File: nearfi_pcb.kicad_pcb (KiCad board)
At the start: 4 copper layers, 45.6 x 45.6 mm, 50 parts, among them J1 PWR_CNN, J2 PROG_CNN, Q1 MMBT3904, SW1 SRST_BTN, U2 TLV1117-33, U3 AT24CS02-STUM, U4 TPL5010, U5 ESP32-S3-MINI-1

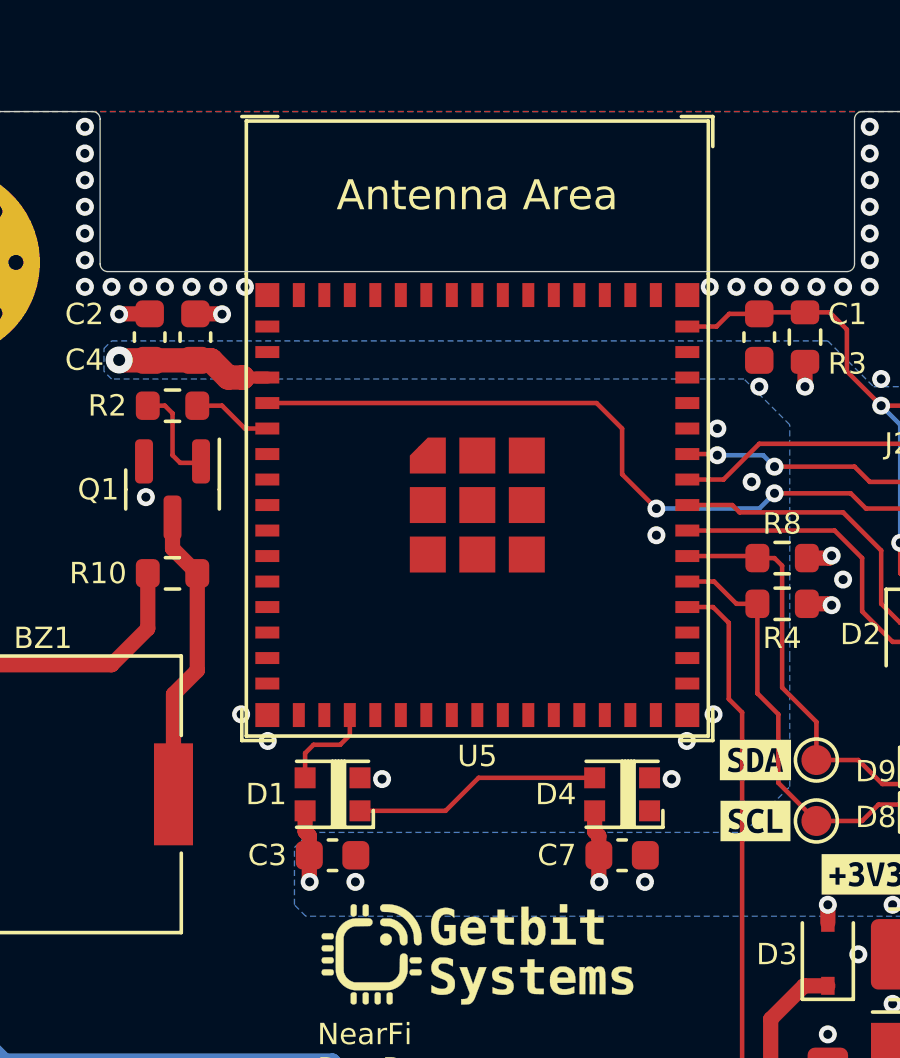
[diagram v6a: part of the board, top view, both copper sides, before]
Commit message: updated to work with kicad v8
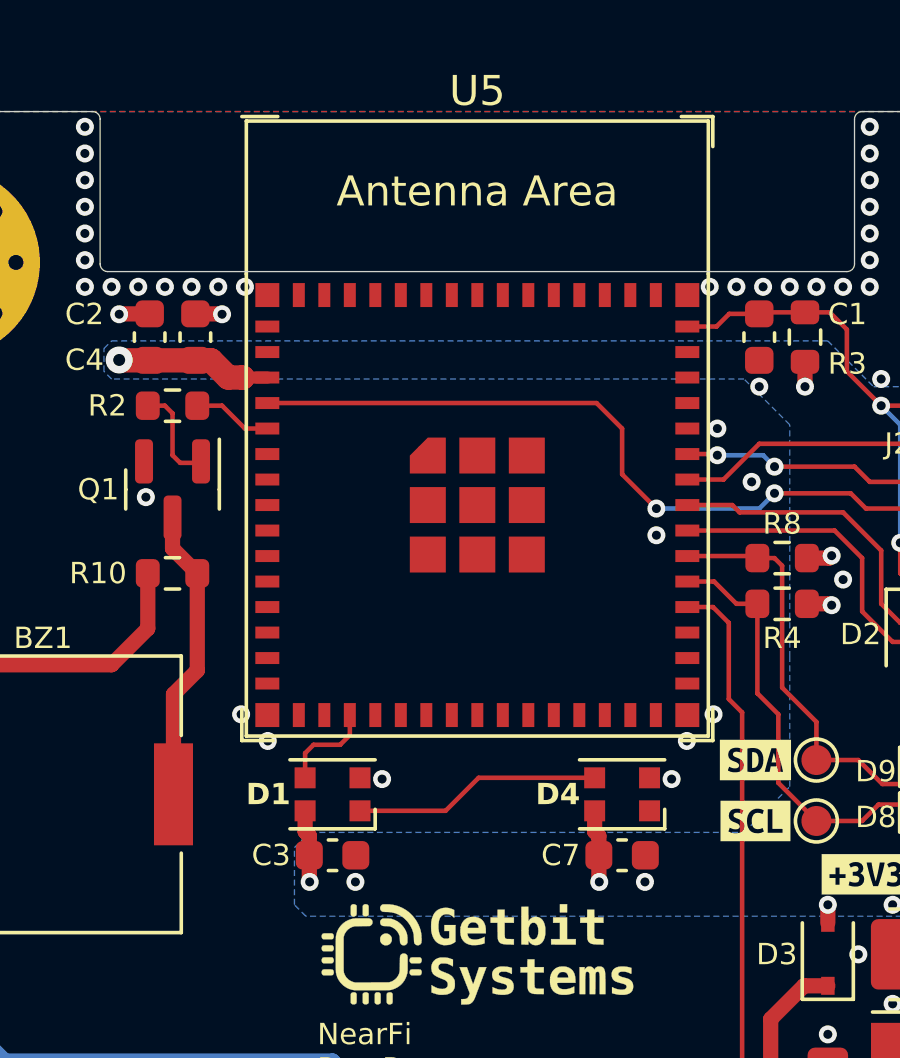
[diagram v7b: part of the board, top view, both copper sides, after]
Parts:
- D1, D4: footprint Misc:WS2812B-2020 -> LED_SMD:LED_WS2812B-2020_PLCC4_2.0x2.0mm
- U5: footprint Espressif:ESP32-S3-MINI-1 -> PCM_Espressif:ESP32-S3-MINI-1
- turned D1 to 180 degrees
- turned D4 to 180 degrees

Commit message: updated schematic and layout
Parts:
- moved C6 35.7 mm to (161.8, 103.9)
- moved D3 35.7 mm to (158.0, 103.9)
- moved D6 35.7 mm to (166.4, 104.6)
- moved G*** 35.7 mm to (146.3, 103.9)
- moved R6 35.7 mm to (156.0, 113.5)
- moved R7 35.7 mm to (166.4, 103.1)
- moved BZ1 35.7 mm to (131.8, 98.5)
- moved C1 35.7 mm to (155.7, 83.3)
- moved C10 35.7 mm to (167.1, 98.5)
- moved C2 35.7 mm to (135.4, 83.3)
- moved C4 35.7 mm to (136.9, 83.3)
- moved D1 35.7 mm to (141.5, 98.5)
- moved D4 35.7 mm to (151.1, 98.5)
- moved D8 35.7 mm to (160.8, 99.3)
- moved D9 35.7 mm to (160.8, 97.8)
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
